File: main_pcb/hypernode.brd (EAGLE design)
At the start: 92.5 x 100 mm, 31 parts, among them IC1 74HCT245D, U1 MAX488, X2 JST-XH-CONNECTOR-02-PIN, X4 JST-XH-CONNECTOR-02-PIN, X7 JST-XH-03-PIN-LONG-PAD, X8 JST-XH-03-PIN-LONG-PAD

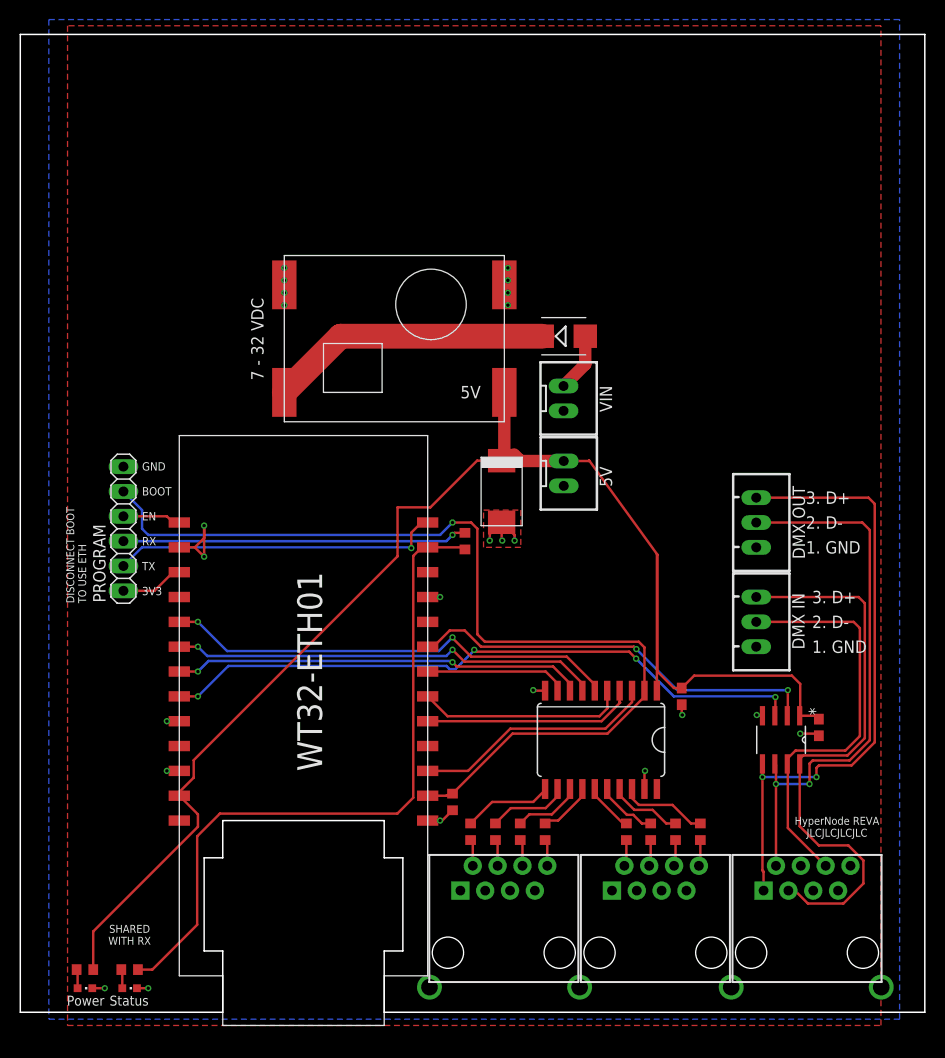
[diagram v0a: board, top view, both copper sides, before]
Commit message: align front panel
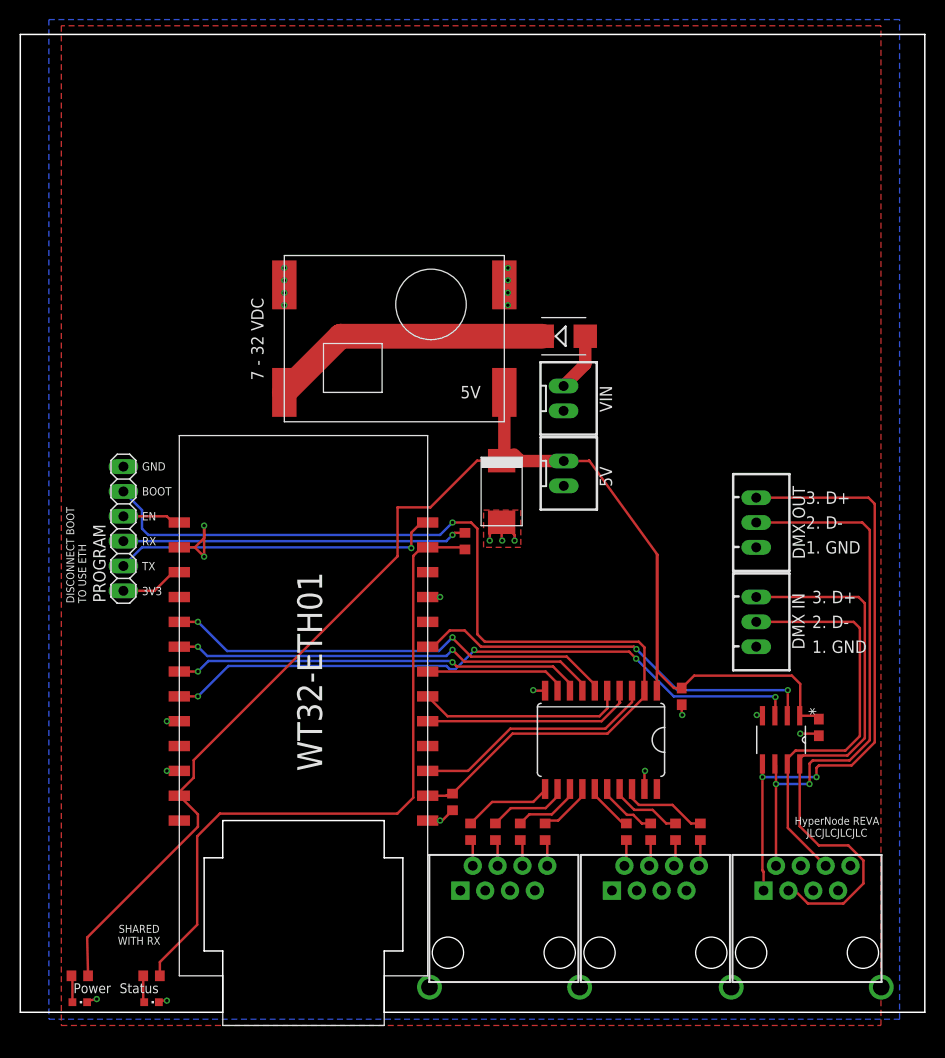
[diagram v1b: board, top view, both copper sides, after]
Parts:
- moved LED_STATUS 2.66 mm to (15.7, 1.03)
- moved R6 2.33 mm to (15.7, 3.73)
- moved LED_PWR 1.52 mm to (8.33, 1.03)
- moved R51 0.83 mm to (8.33, 3.73)
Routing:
- net RX: track 71.2 -> 70.0 mm
- net +5V: track 150.5 -> 151.4 mm
- net N$2: track 1.95 -> 2.74 mm
- net N$34: track 1.95 -> 2.74 mm

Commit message: rev A
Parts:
- moved U$4 76.2 mm to (10.8, 36.8)
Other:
- board text added: "FRONT PANEL WIDTH"

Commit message: fix boot connetion
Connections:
- new net IO0: PROGRAM.5, U$17.P_IO0
- net WS4: no longer PROGRAM.5
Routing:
- net WS4: track 99.8 -> 27.0 mm, vias 1 -> 0
- net IO0: track 0.00 -> 49.3 mm, vias 0 -> 1
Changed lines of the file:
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@@
 </element>
 <element name="R5" library="Multischriever" package="ADAFRUIT_R0603" value="1K" x="47.72" y="48.18" smashed="yes" rot="R270">
-<attribute name="VALUE" x="46.45" y="48.18" size="0.8128" layer="27" font="vector" rot="R270" align="center"/>
+<attribute name="VALUE" x="46.45" y="47.545" size="0.8128" layer="27" font="vector" rot="R270" align="center"/>
 </element>
 </elements>
@@
 </polygon>
 <wire x1="18.51" y1="22.5205875" x2="18.51" y2="22.145" width="0.254" layer="1"/>
-<wire x1="19.9832" y1="23.9937875" x2="18.51" y2="22.5205875" width="0.254" layer="1"/>
-<wire x1="19.9832" y1="25.7826125" x2="40.8311875" y2="46.6306" width="0.254" layer="1"/>
-<wire x1="19.9832" y1="25.7826125" x2="19.9832" y2="23.9937875" width="0.254" layer="1"/>
+<wire x1="20.6182" y1="24.6287875" x2="18.51" y2="22.5205875" width="0.254" layer="1"/>
+<wire x1="20.6182" y1="26.4176125" x2="40.8311875" y2="46.6306" width="0.254" layer="1"/>
+<wire x1="20.6182" y1="26.4176125" x2="20.6182" y2="24.6287875" width="0.254" layer="1"/>
 <wire x1="40.8311875" y1="46.6306" x2="40.8311875" y2="51.6344" width="0.254" layer="1"/>
 <wire x1="40.8311875" y1="51.6344" x2="44.1894" y2="51.6344" width="0.254" layer="1"/>
@@
 <wire x1="52.585" y1="28.495" x2="46.45" y2="22.36" width="0.254" layer="1"/>
 <wire x1="62.3008125" y1="28.495" x2="52.585" y2="28.495" width="0.254" layer="1"/>
-<contactref element="PROGRAM" pad="5"/>
-<wire x1="45.18" y1="48.815" x2="15.97" y2="48.815" width="0.254" layer="16"/>
-<wire x1="45.18" y1="48.815" x2="46.45" y2="50.085" width="0.254" layer="16"/>
-<via x="46.45" y="50.085" extent="1-16" drill="0.35"/>
-<wire x1="46.45" y1="50.085" x2="48.355" y2="50.085" width="0.254" layer="1"/>
-<wire x1="48.355" y1="50.085" x2="48.99" y2="49.45" width="0.254" layer="1"/>
-<wire x1="48.99" y1="49.45" x2="48.99" y2="38.655" width="0.254" layer="1"/>
-<wire x1="49.752" y1="37.893" x2="65.5" y2="37.893" width="0.254" layer="1"/>
-<wire x1="66.08" y1="32.8892" x2="66.08" y2="37.313" width="0.254" layer="1"/>
-<wire x1="66.08" y1="37.313" x2="65.5" y2="37.893" width="0.254" layer="1"/>
-<wire x1="48.99" y1="38.655" x2="49.752" y2="37.893" width="0.254" layer="1"/>
-<wire x1="15.24" y1="49.545" x2="15.24" y2="51.435" width="0.254" layer="16"/>
-<wire x1="15.24" y1="51.435" x2="13.415" y2="53.26" width="0.254" layer="16"/>
-<wire x1="13.415" y1="53.26" x2="12.795" y2="53.26" width="0.254" layer="16"/>
-<wire x1="15.97" y1="48.815" x2="15.24" y2="49.545" width="0.254" layer="16"/>
 </signal>
 <signal name="WS5">
@@
 <contactref element="U$17" pad="P_3V3@1"/>
 </signal>
+<signal name="IO0">
+<contactref element="U$17" pad="P_IO0"/>
+<contactref element="PROGRAM" pad="5"/>
+<wire x1="12.795" y1="53.26" x2="13.89" y2="53.26" width="0.254" layer="16"/>
+<wire x1="13.89" y1="53.26" x2="13.97" y2="53.34" width="0.254" layer="16"/>
+<wire x1="13.97" y1="53.34" x2="15.24" y2="52.07" width="0.254" layer="16"/>
+<wire x1="15.24" y1="52.07" x2="15.24" y2="49.53" width="0.254" layer="16"/>
+<wire x1="15.24" y1="49.53" x2="15.875" y2="48.895" width="0.254" layer="16"/>
+<wire x1="15.875" y1="48.895" x2="45.085" y2="48.895" width="0.254" layer="16"/>
+<via x="46.355" y="50.165" extent="1-16" drill="0.35"/>
+<wire x1="46.355" y1="50.165" x2="48.26" y2="50.165" width="0.254" layer="1"/>
+<wire x1="48.26" y1="50.165" x2="48.895" y2="49.53" width="0.254" layer="1"/>
+<wire x1="48.18" y1="45.005" x2="43.91" y2="45.005" width="0.254" layer="1"/>
+<wire x1="45.085" y1="48.895" x2="46.355" y2="50.165" width="0.254" layer="16"/>
+<wire x1="48.895" y1="49.53" x2="48.895" y2="45.72" width="0.254" layer="1"/>
+<wire x1="48.895" y1="45.72" x2="48.18" y2="45.005" width="0.254" layer="1"/>
+</signal>
 </signals>

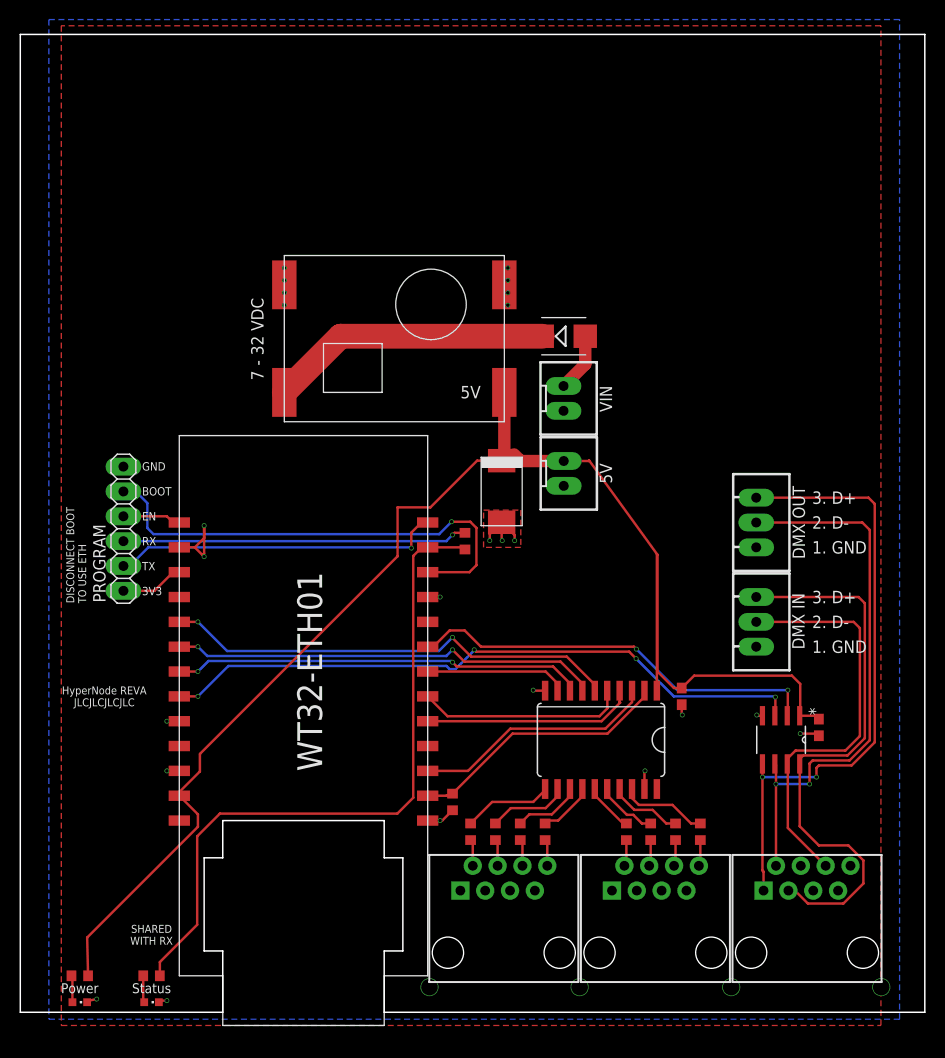
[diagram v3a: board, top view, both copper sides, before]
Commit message: move wrt32 away from ws2812 ports
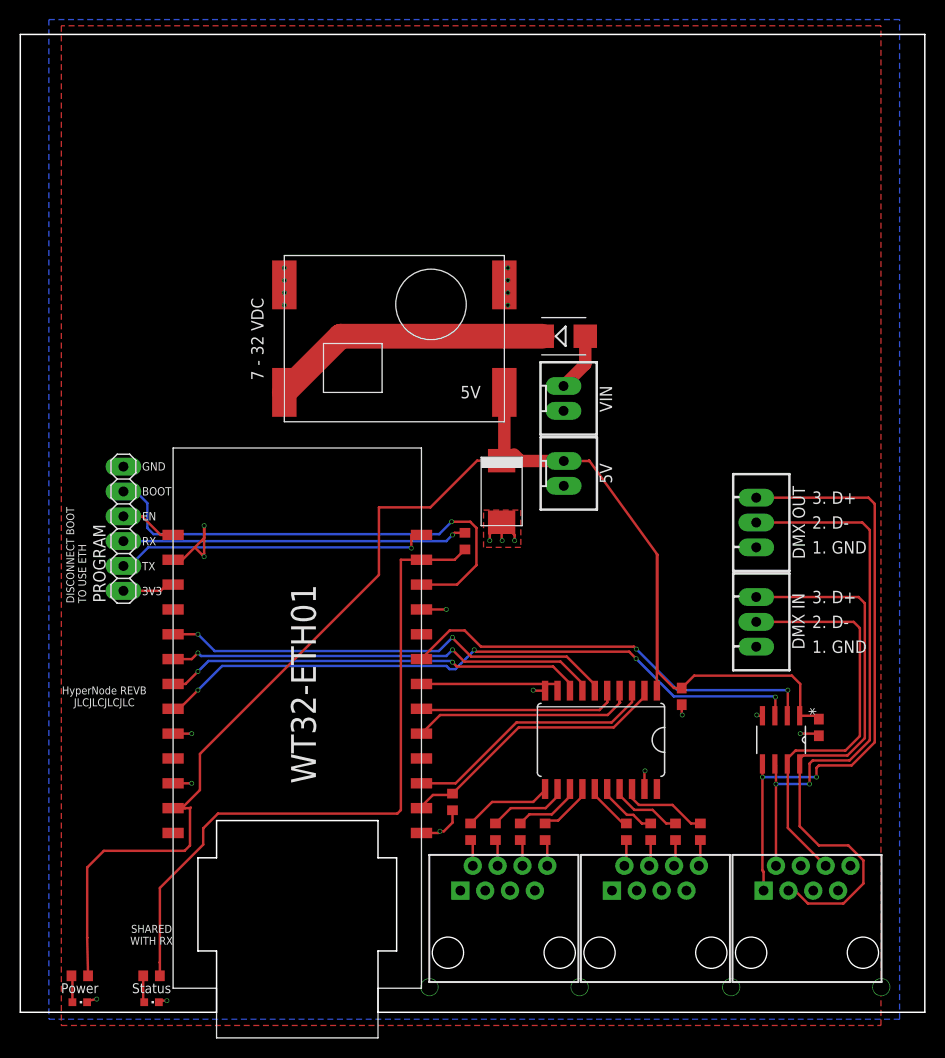
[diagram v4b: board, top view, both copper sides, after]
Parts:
- moved U$17 1.42 mm to (18.5, 48.8)
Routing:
- net +5V: track 151.4 -> 160.4 mm
- net GND: track 33.7 -> 40.0 mm
- net WS4: track 27.0 -> 28.3 mm
- net TX: track 33.9 -> 32.6 mm
- net DMXIN: track 42.7 -> 43.9 mm
- net DMXOUT: track 67.2 -> 68.4 mm
- net +3V3: track 6.50 -> 5.34 mm
- net WS6: track 42.1 -> 43.3 mm
- net WS3: track 25.0 -> 26.1 mm
- net WS2: track 21.7 -> 22.9 mm
- net IO0: track 49.3 -> 50.5 mm
- net WS1: track 21.4 -> 20.6 mm
- net WS7: track 44.1 -> 44.7 mm
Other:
- outline, holes or cut-outs redrawn
- board text added: "HyperNode REVB JLCJLCJLCJLC"
- board text removed: "HyperNode REVA JLCJLCJLCJLC"

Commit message: DRC and cleanup
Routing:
- net +5V: track 160.4 -> 170.4 mm
- net GND: track 40.0 -> 35.8 mm
- net WS5: track 14.7 -> 15.7 mm

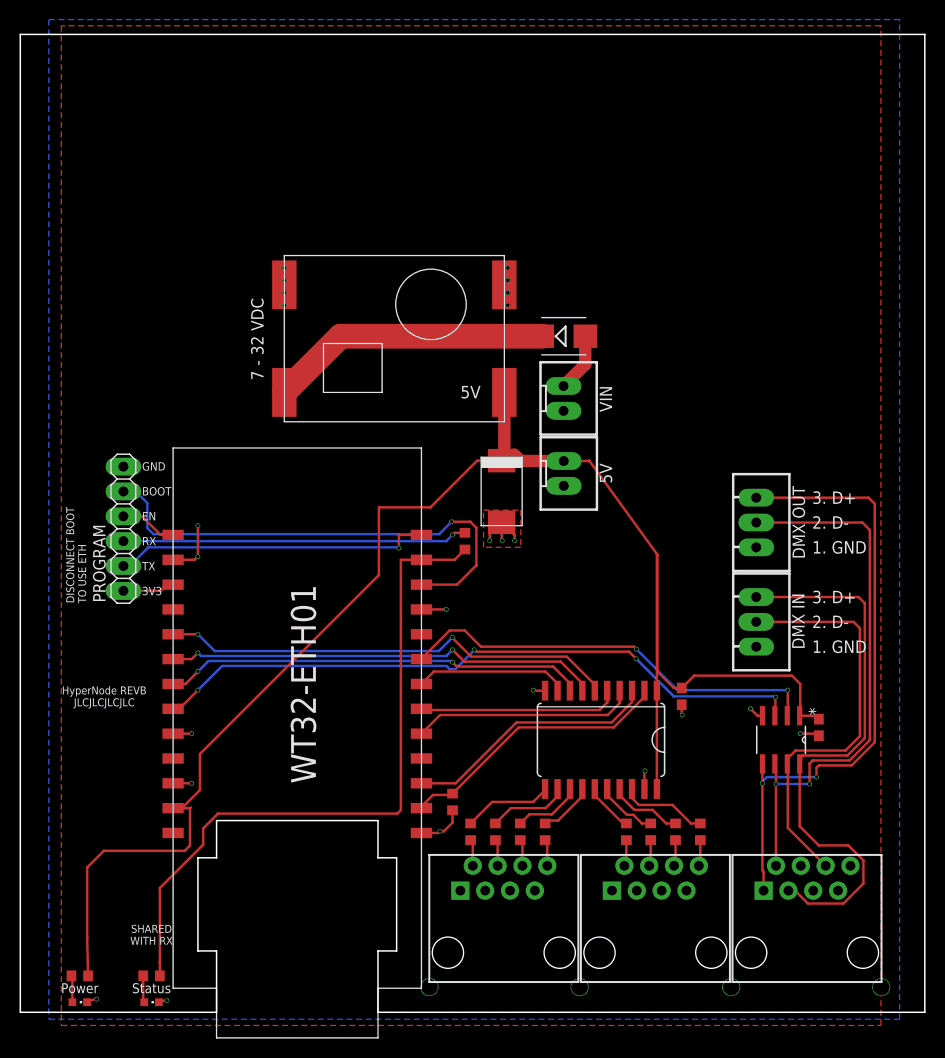
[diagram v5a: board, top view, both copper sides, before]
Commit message: tented vias
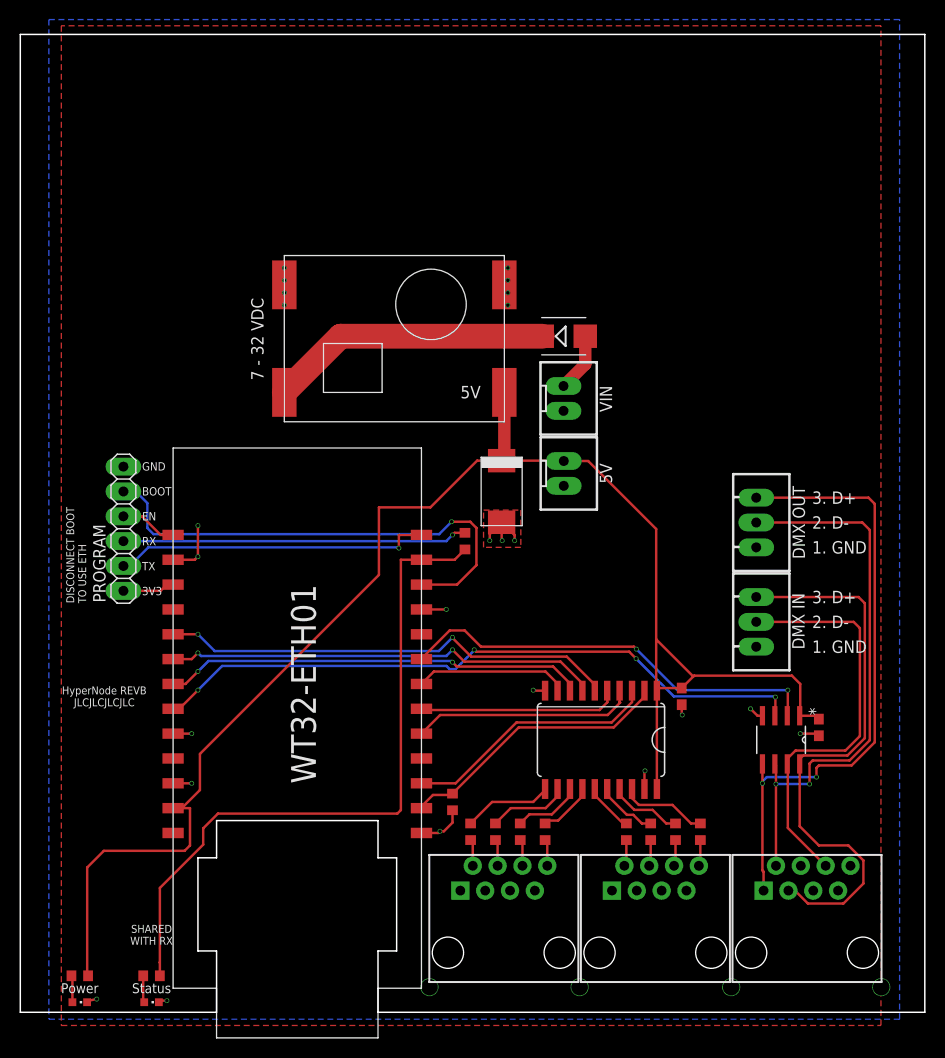
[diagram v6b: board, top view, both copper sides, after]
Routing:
- net +5V: track 170.4 -> 162.1 mm
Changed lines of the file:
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@@
 <setting verticaltext="up"/>
 </settings>
-<grid distance="25" unitdist="mil" unit="mm" style="lines" multiple="1" display="yes" altdistance="6.25" altunitdist="mil" altunit="mm"/>
+<grid distance="25" unitdist="mil" unit="mil" style="lines" multiple="1" display="yes" altdistance="6.25" altunitdist="mil" altunit="mil"/>
 <layers>
 <layer number="1" name="Top" color="4" fill="1" visible="yes" active="yes"/>
@@
 </class>
 </classes>
-<designrules name="jlcpcb-2layers">
+<designrules name="jlcpcb-2layers *">
 <description language="en">&lt;b&gt;JLCPCB design rules (2 layers)&lt;/b&gt;
 &lt;ul&gt;
@@
 <param name="mlMinCreamFrame" value="0mil"/>
 <param name="mlMaxCreamFrame" value="0mil"/>
-<param name="mlViaStopLimit" value="0mil"/>
+<param name="mlViaStopLimit" value="15mil"/>
 <param name="srRoundness" value="0"/>
 <param name="srMinRoundness" value="0mil"/>
@@
 <contactref element="R51" pad="2"/>
 <contactref element="X4" pad="1"/>
-<wire x1="57.825" y1="56.375" x2="52.145" y2="56.375" width="1.27" layer="1"/>
-<wire x1="52.745" y1="57.045" x2="53.415" y2="56.375" width="1.27" layer="1"/>
 <contactref element="U$17" pad="P_5V"/>
 <contactref element="C2" pad="1"/>
@@
 <wire x1="48.965" y1="56.41" x2="51.475" y2="56.41" width="0.254" layer="1"/>
 <wire x1="44.1894" y1="51.6344" x2="48.965" y2="56.41" width="0.254" layer="1"/>
-<wire x1="17.875" y1="20.875" x2="19.145" y2="20.875" width="0.254" layer="1"/>
-<wire x1="67.35" y1="46.85" x2="67.35" y2="32.8892" width="0.254" layer="1"/>
-<wire x1="57.825" y1="56.375" x2="60.36" y2="56.375" width="0.254" layer="1"/>
-<wire x1="60.36" y1="56.375" x2="60.42" y2="56.435" width="0.254" layer="1"/>
-<wire x1="60.42" y1="56.435" x2="67.405" y2="46.795" width="0.254" layer="1"/>
-<wire x1="67.405" y1="46.795" x2="67.405" y2="34.845" width="0.254" layer="1"/>
-<wire x1="67.405" y1="34.845" x2="69.095" y2="33.155" width="0.254" layer="1"/>
-<wire x1="69.095" y1="33.155" x2="69.89" y2="33.155" width="0.254" layer="1"/>
-<wire x1="69.89" y1="33.155" x2="71.16" y2="34.425" width="0.254" layer="1"/>
+<wire x1="69.89" y1="33.155" x2="71.0725" y2="34.3375" width="0.254" layer="1"/>
+<wire x1="71.0725" y1="34.3375" x2="71.16" y2="34.425" width="0.254" layer="1"/>
 <wire x1="81.16" y1="34.425" x2="71.16" y2="34.425" width="0.254" layer="1"/>
 <wire x1="81.16" y1="34.425" x2="82.01" y2="33.575" width="0.254" layer="1"/>
 <wire x1="82.01" y1="33.575" x2="82.01" y2="30.3238" width="0.254" layer="1"/>
-<wire x1="9.08764375" y1="7.64264375" x2="9.08806875" y2="7.624675" width="0.254" layer="1"/>
-<wire x1="9.08806875" y1="7.624675" x2="9.18" y2="3.73" width="0.254" layer="1"/>
-<wire x1="17.875" y1="20.875" x2="19.605" y2="20.875" width="0.254" layer="1"/>
-<wire x1="19.605" y1="20.875" x2="19.685" y2="20.955" width="0.254" layer="1"/>
-<wire x1="19.605" y1="20.875" x2="19.605" y2="17.065" width="0.254" layer="1"/>
+<wire x1="19.605" y1="17.065" x2="19.605" y2="20.875" width="0.254" layer="1"/>
 <wire x1="19.605" y1="17.065" x2="19.05" y2="16.51" width="0.254" layer="1"/>
 <wire x1="19.05" y1="16.51" x2="10.795" y2="16.51" width="0.254" layer="1"/>
 <wire x1="10.795" y1="16.51" x2="9.08806875" y2="14.80306875" width="0.254" layer="1"/>
-<wire x1="9.08806875" y1="14.80306875" x2="9.08806875" y2="7.624675" width="0.254" layer="1"/>
 <wire x1="67.35" y1="32.8892" x2="67.35" y2="22.8308" width="0.254" layer="1"/>
+<wire x1="19.605" y1="20.875" x2="17.875" y2="20.875" width="0.254" layer="1"/>
+<wire x1="9.08806875" y1="14.80306875" x2="9.08806875" y2="3.82193125" width="0.254" layer="1"/>
+<wire x1="9.08806875" y1="3.82193125" x2="9.18" y2="3.73" width="0.254" layer="1"/>
+<wire x1="67.27964375" y1="38.1" x2="67.27964375" y2="32.95955625" width="0.254" layer="1"/>
+<wire x1="67.27964375" y1="32.95955625" x2="67.35" y2="32.8892" width="0.254" layer="1"/>
+<wire x1="67.35" y1="32.8892" x2="67.6158" y2="33.155" width="0.254" layer="1"/>
+<wire x1="67.6158" y1="33.155" x2="69.89" y2="33.155" width="0.254" layer="1"/>
+<wire x1="71.0725" y1="34.3375" x2="67.31" y2="38.1" width="0.254" layer="1"/>
+<wire x1="67.31" y1="38.1" x2="67.27964375" y2="38.1" width="0.254" layer="1"/>
+<wire x1="51.475" y1="56.41" x2="57.79" y2="56.41" width="0.254" layer="1"/>
+<wire x1="57.79" y1="56.41" x2="57.825" y2="56.375" width="0.254" layer="1"/>
+<wire x1="67.27964375" y1="49.42035625" x2="60.325" y2="56.375" width="0.254" layer="1"/>
+<wire x1="67.27964375" y1="49.42035625" x2="67.27964375" y2="38.1" width="0.254" layer="1"/>
+<wire x1="60.325" y1="56.375" x2="57.825" y2="56.375" width="0.254" layer="1"/>
 </signal>
 <signal name="DMXB">
